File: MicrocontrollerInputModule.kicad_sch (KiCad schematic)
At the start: 50 parts, among them J1 Conn_02x04_Odd_Even, J2 IPEX 20655-045E-01, U1 W25Q16JVUXIQ, U2 RP2040, U3 MCP23S17_ML, Y1 12.000MHz

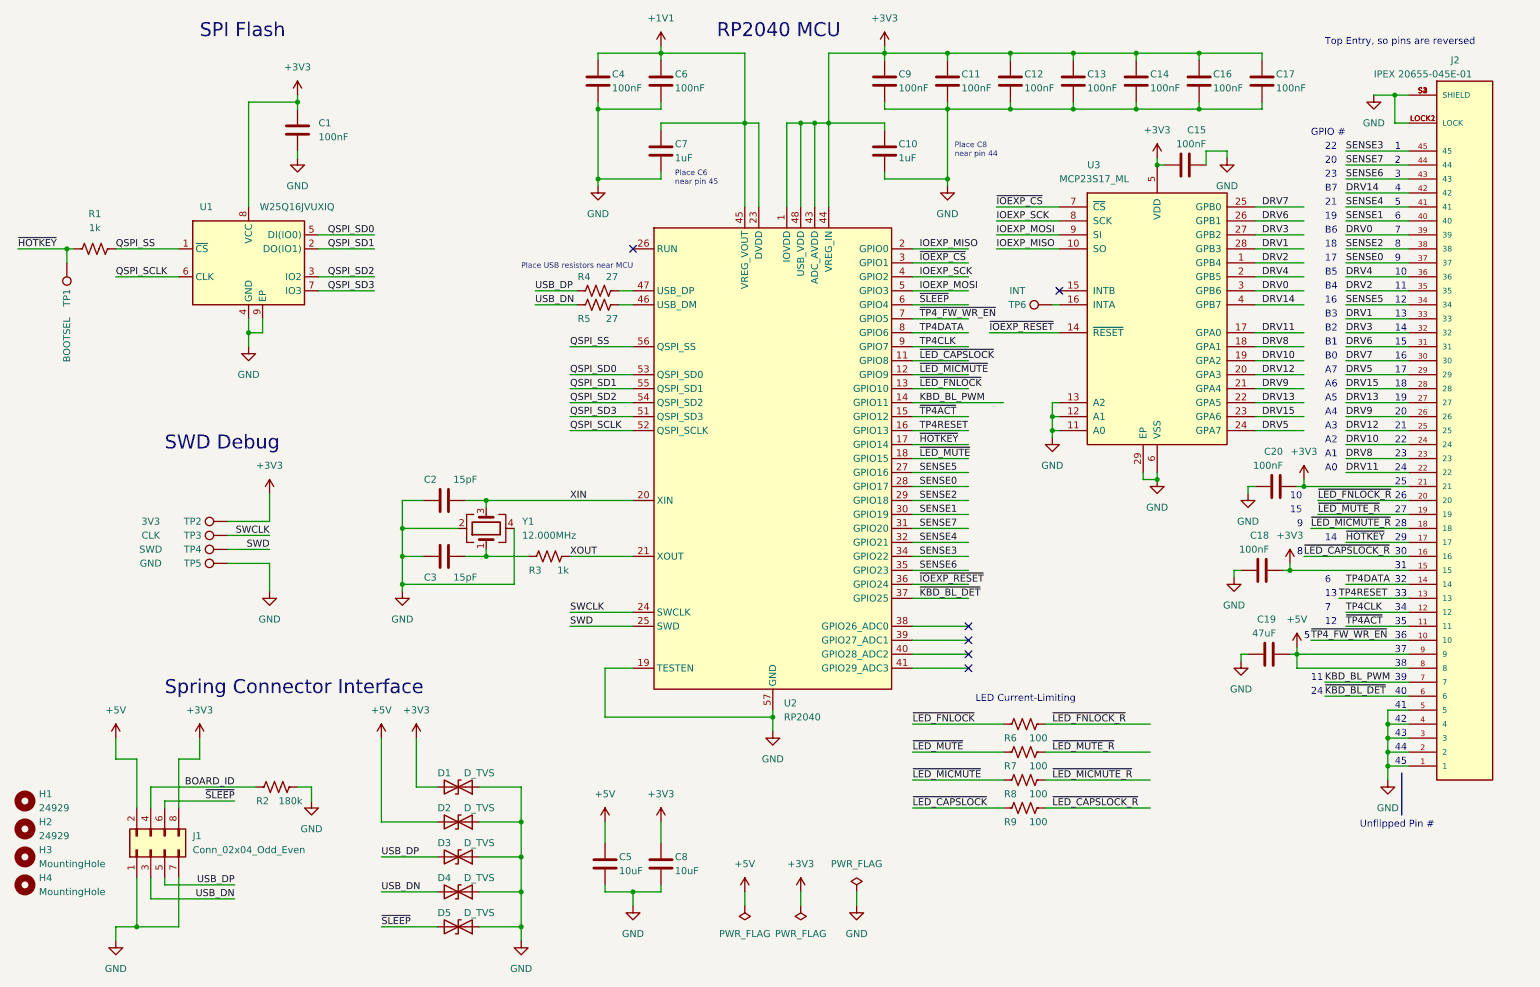
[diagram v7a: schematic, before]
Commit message: Version sent to JLCPCB for assembly 2024-01-29
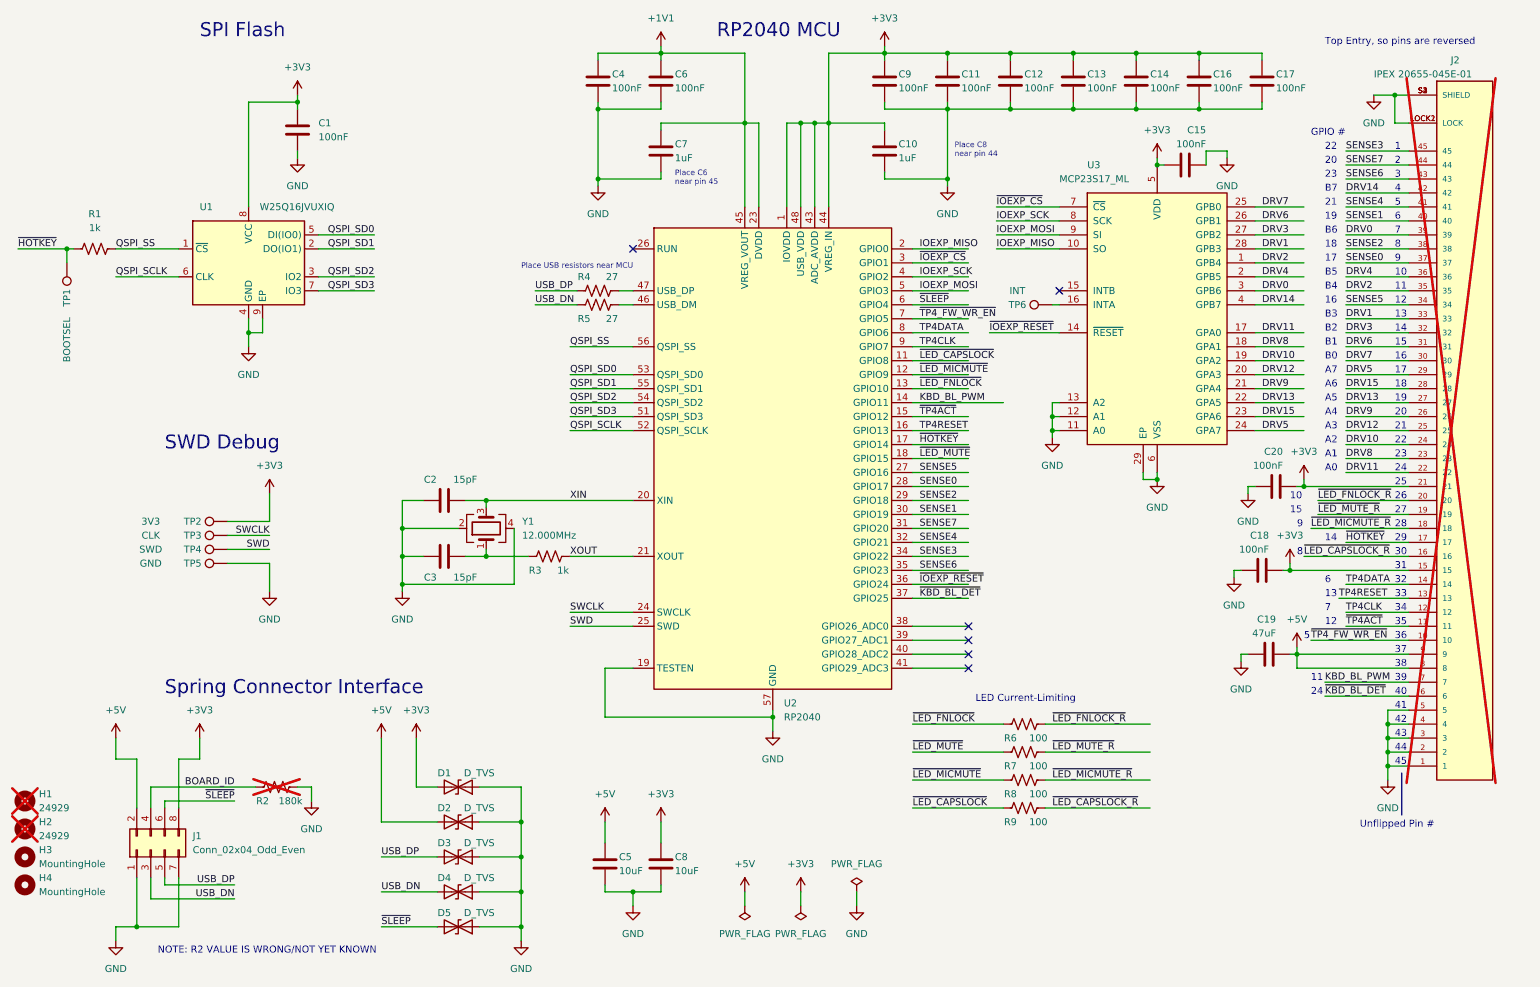
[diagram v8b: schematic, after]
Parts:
- H1, H2, J2, R2: now not fitted
- H3, H4, J1, TP1, TP2, TP3, TP4, TP5, TP6: now left out of the parts list
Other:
- note added: "NOTE: R2 VALUE IS WRONG/NOT YET KNOWN"
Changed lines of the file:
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@@
     (effects (font (size 1.27 1.27)) (justify left bottom))
   )
+  (text "NOTE: R2 VALUE IS WRONG/NOT YET KNOWN" (at 40.64 187.96 0)
+    (effects (font (size 1.27 1.27)) (justify left bottom))
+  )
   (text "32" (at 265.43 120.65 0)
     (effects (font (size 1.27 1.27)) (justify left bottom))
@@
   )
   (symbol (lib_id "Connector:TestPoint") (at 53.34 109.22 90) (unit 1)
-    (in_bom yes) (on_board yes) (dnp no)
+    (in_bom no) (on_board yes) (dnp no)
     (property "Reference" "TP2" (at 46.99 109.22 90)
       (effects (font (size 1.27 1.27)))
@@
   )
   (symbol (lib_id "Connector_Generic:Conn_02x04_Odd_Even") (at 39.37 168.91 90) (unit 1)
-    (in_bom yes) (on_board yes) (dnp no) (fields_autoplaced)
+    (in_bom no) (on_board yes) (dnp no) (fields_autoplaced)
     (property "Reference" "J1" (at 46.99 166.3699 90)
       (effects (font (size 1.27 1.27)) (justify right))
@@
   )
   (symbol (lib_id "Connector:TestPoint") (at 53.34 114.3 90) (unit 1)
-    (in_bom yes) (on_board yes) (dnp no)
+    (in_bom no) (on_board yes) (dnp no)
     (property "Reference" "TP4" (at 46.99 114.3 90)
       (effects (font (size 1.27 1.27)))
@@
   )
   (symbol (lib_id "Mechanical:MountingHole") (at 16.51 170.18 0) (unit 1)
-    (in_bom yes) (on_board yes) (dnp no)
+    (in_bom no) (on_board yes) (dnp no)
     (property "Reference" "H3" (at 19.05 168.91 0)
       (effects (font (size 1.27 1.27)) (justify left))
@@
   )
   (symbol (lib_id "Connector:TestPoint") (at 24.13 62.23 180) (unit 1)
-    (in_bom yes) (on_board yes) (dnp no)
+    (in_bom no) (on_board yes) (dnp no)
     (property "Reference" "TP1" (at 24.13 68.58 90)
       (effects (font (size 1.27 1.27)))
@@
   )
   (symbol (lib_id "Connector:TestPoint") (at 53.34 116.84 90) (unit 1)
-    (in_bom yes) (on_board yes) (dnp no)
+    (in_bom no) (on_board yes) (dnp no)
     (property "Reference" "TP5" (at 46.99 116.84 90)
       (effects (font (size 1.27 1.27)))
@@
   )
   (symbol (lib_id "Device:R_US") (at 62.23 157.48 90) (unit 1)
-    (in_bom yes) (on_board yes) (dnp no)
+    (in_bom yes) (on_board yes) (dnp yes)
     (property "Reference" "R2" (at 59.69 160.02 90)
       (effects (font (size 1.27 1.27)))
@@
   )
   (symbol (lib_id "Connector:TestPoint") (at 53.34 111.76 90) (unit 1)
-    (in_bom yes) (on_board yes) (dnp no)
+    (in_bom no) (on_board yes) (dnp no)
     (property "Reference" "TP3" (at 46.99 111.76 90)
       (effects (font (size 1.27 1.27)))
@@
   )
   (symbol (lib_id "Mechanical:MountingHole") (at 16.51 160.02 0) (unit 1)
-    (in_bom yes) (on_board yes) (dnp no)
+    (in_bom yes) (on_board yes) (dnp yes)
     (property "Reference" "H1" (at 19.05 158.75 0)
       (effects (font (size 1.27 1.27)) (justify left))
@@
   )
   (symbol (lib_id "Connector:TestPoint") (at 203.2 69.85 90) (unit 1)
-    (in_bom yes) (on_board yes) (dnp no)
+    (in_bom no) (on_board yes) (dnp no)
     (property "Reference" "TP6" (at 196.85 69.85 90)
       (effects (font (size 1.27 1.27)))
@@
   )
   (symbol (lib_id "Mechanical:MountingHole") (at 16.51 175.26 0) (unit 1)
-    (in_bom yes) (on_board yes) (dnp no)
+    (in_bom no) (on_board yes) (dnp no)
     (property "Reference" "H4" (at 19.05 173.99 0)
       (effects (font (size 1.27 1.27)) (justify left))
@@
   )
   (symbol (lib_id "20655-045E-01:20655-045E-01") (at 278.13 92.71 0) (mirror x) (unit 1)
-    (in_bom yes) (on_board yes) (dnp no)
+    (in_bom yes) (on_board yes) (dnp yes)
     (property "Reference" "J2" (at 275.59 25.4 0)
       (effects (font (size 1.27 1.27)) (justify left))
@@
   )
   (symbol (lib_id "Mechanical:MountingHole") (at 16.51 165.1 0) (unit 1)
-    (in_bom yes) (on_board yes) (dnp no)
+    (in_bom yes) (on_board yes) (dnp yes)
     (property "Reference" "H2" (at 19.05 163.83 0)
       (effects (font (size 1.27 1.27)) (justify left))
